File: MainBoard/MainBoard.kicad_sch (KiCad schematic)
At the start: 30 parts, among them J1 1761681-3, Q1 BC557, Q2 BC557, Q3 BC557, Q4 BC557, Q5 BC547, Q6 BC547, Q7 BC547, Q8 BC547

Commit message: snapshot
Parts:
- added R5: 470k, symbol Device:R
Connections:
- net NonInvertingInput: now also R5.1
- net Output: now also R5.2
- net DiffPair renamed InputStage
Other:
- moved on the sheet: D3, D4, D5, D6, Q1, Q2, Q3, Q4, Q5, Q6, Q7, Q8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

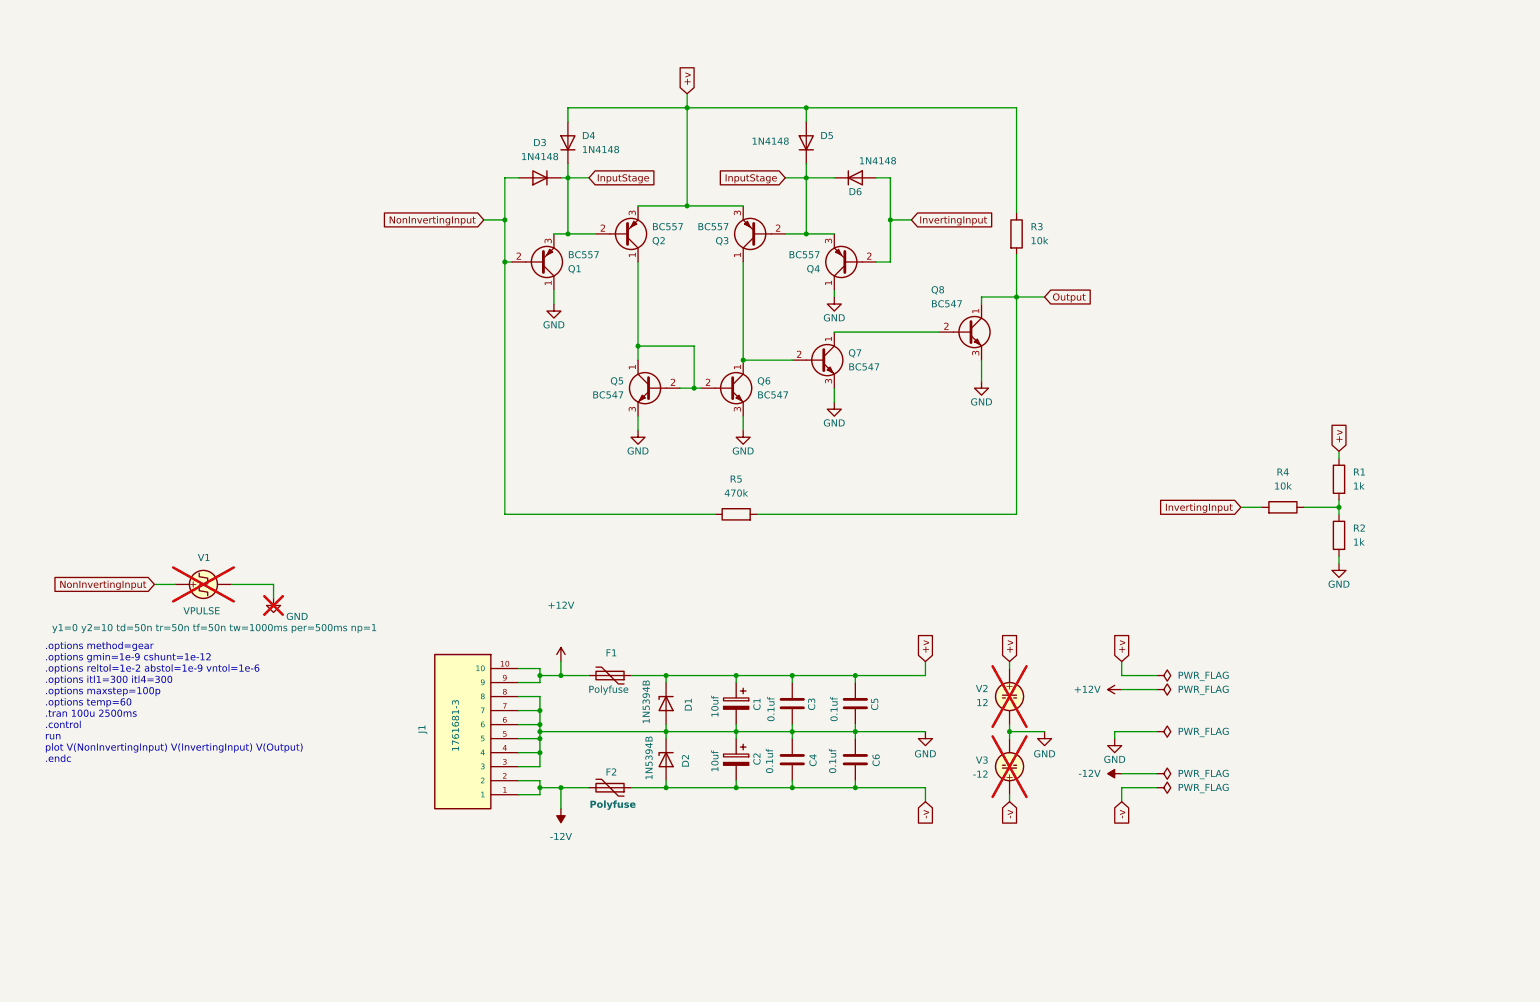
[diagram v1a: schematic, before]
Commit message: corrected input stage
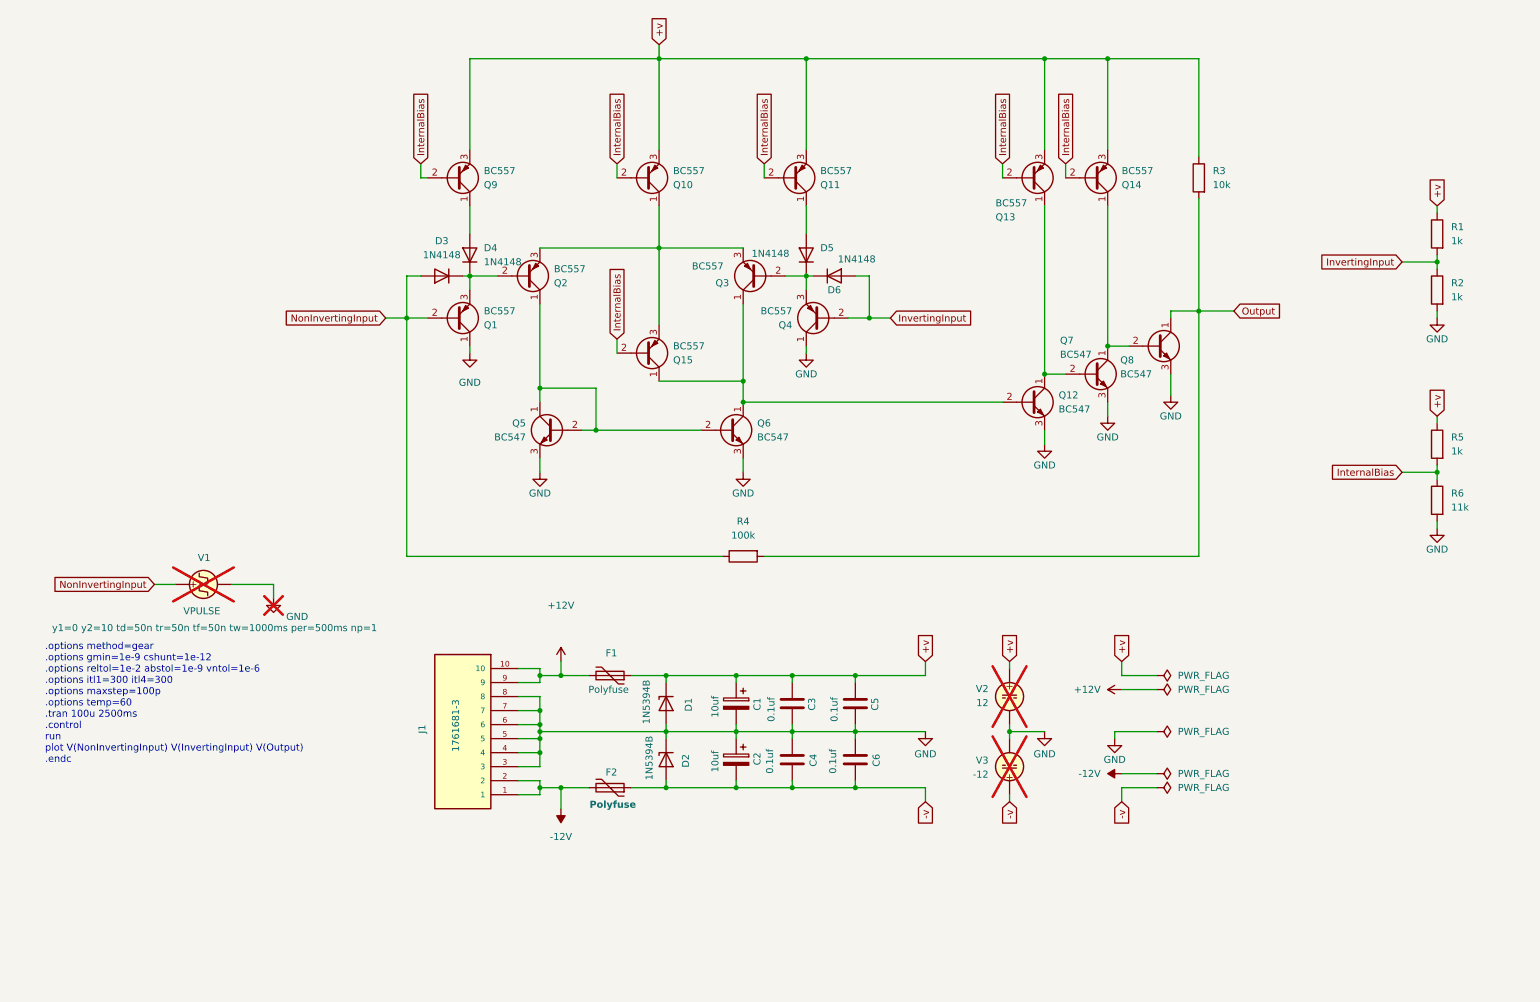
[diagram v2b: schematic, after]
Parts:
- added Q10, Q11, Q13, Q14, Q15, Q9: BC557, Package_TO_SOT_THT:TO-92_Inline, symbol Transistor_BJT:BC557
- added Q12: BC547, Package_TO_SOT_THT:TO-92_Inline, symbol Transistor_BJT:BC547
- added R6: 11k, symbol Device:R
- R4: value 10k -> 100k
- R5: value 470k -> 1k
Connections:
- net +v: now also R5.1, Q10.3 (E), Q11.3 (E), Q13.3 (E), Q14.3 (E), Q9.3 (E); no longer D4.2 (A), D5.2 (A), Q2.3 (E), Q3.3 (E)
- net GND: now also Q12.3 (E), R6.2
- net InvertingInput: now also R1.2, R2.1; no longer R4.2
- net NonInvertingInput: now also R4.1; no longer R5.1
- net Output: now also R4.2; no longer R5.2
- net at Q7.1 (C), Q8.2 (B): now also Q14.1 (C)
- net at Q3.1 (C), Q6.1 (C): now also Q12.2 (B), Q15.1 (C); no longer Q7.2 (B)
- net InputStage: no longer names the net of D3.1 (K), D4.1 (K), Q1.3 (E), Q2.2 (B)
- net InputStage: no longer D5.1 (K), D6.1 (K), Q3.2 (B), Q4.3 (E)
- new net: Q12.1 (C), Q13.1 (C), Q7.2 (B)
- new net: D4.2 (A), Q9.1 (C)
- new net: D5.1 (K), D6.1 (K), Q3.2 (B), Q4.3 (E)
- new net: Q10.1 (C), Q15.3 (E), Q2.3 (E), Q3.3 (E)
- new net: D5.2 (A), Q11.1 (C)
- new net InternalBias: Q10.2 (B), Q11.2 (B), Q13.2 (B), Q14.2 (B), Q15.2 (B), Q9.2 (B), R5.2, R6.1
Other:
- moved on the sheet: D3, D4, D5, D6, Q1, Q2, Q3, Q4, Q5, Q6, Q7, Q8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

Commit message: adjusted simulation paramters
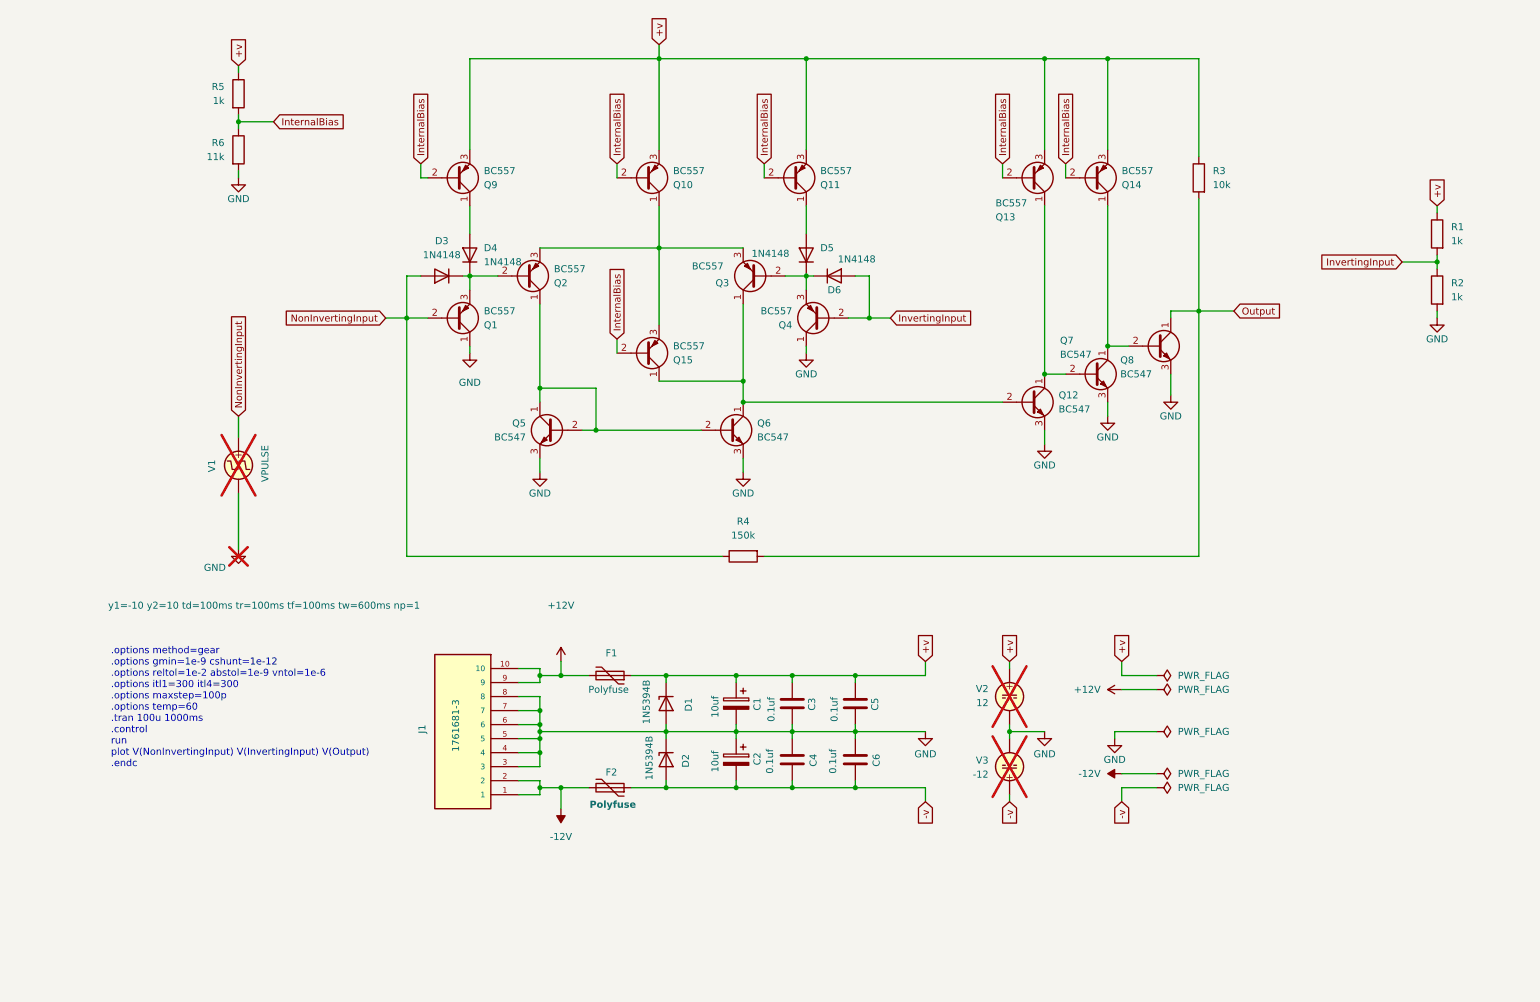
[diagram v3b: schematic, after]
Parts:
- R4: value 100k -> 150k
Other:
- note added: ".options method=gear .options gmin=1e-9 cshunt=1e-12 .options reltol=1e-2 abstol=1e-9 vntol=1e-6 .options itl1=300 itl4=300 .options maxstep=100p .options temp=60 .tran 100u 1000ms .control run plot V(NonInvertingInput) V(InvertingInput) V(Output) .endc"
- note removed: ".options method=gear .options gmin=1e-9 cshunt=1e-12 .options reltol=1e-2 abstol=1e-9 vntol=1e-6 .options itl1=300 itl4=300 .options maxstep=100p .options temp=60 .tran 100u 2500ms .control run plot V(NonInvertingInput) V(InvertingInput) V(Output) .endc"
- moved on the sheet: R5, R6, V1
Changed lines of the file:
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@@
 	(generator_version "9.0")
 	(paper "A4")
-	(text ".options method=gear \n.options gmin=1e-9 cshunt=1e-12 \n.options reltol=1e-2 abstol=1e-9 vntol=1e-6 \n.options itl1=300 itl4=300 \n.options maxstep=100p\n.options temp=60\n.tran 100u 2500ms\n.control\nrun\nplot V(NonInvertingInput) V(InvertingInput) V(Output)\n.endc"
+	(text ".options method=gear \n.options gmin=1e-9 cshunt=1e-12 \n.options reltol=1e-2 abstol=1e-9 vntol=1e-6 \n.options itl1=300 itl4=300 \n.options maxstep=100p\n.options temp=60\n.tran 100u 1000ms\n.control\nrun\nplot V(NonInvertingInput) V(InvertingInput) V(Output)\n.endc"
 		(exclude_from_sim no)
-		(at 19.558 138.43 0)
+		(at 31.496 139.192 0)
 		(effects
 			(font
@@
 	)
 	(junction
-		(at 271.78 96.52)
+		(at 54.61 33.02)
 		(diameter 0)
 		(color 0 0 0 0)
@@
 	(wire
 		(pts
-			(xy 271.78 96.52) (xy 265.43 96.52)
+			(xy 54.61 33.02) (xy 60.96 33.02)
 		)
 		(stroke
@@
 	(wire
 		(pts
-			(xy 60.96 116.84) (xy 60.96 119.38)
-		)
-		(stroke
-			(width 0)
-			(type default)
-		)
-	)
-	(wire
-		(pts
 			(xy 153.67 60.96) (xy 157.48 60.96)
 		)
@@
 	(wire
 		(pts
-			(xy 271.78 95.25) (xy 271.78 96.52)
+			(xy 54.61 31.75) (xy 54.61 33.02)
 		)
 		(stroke
@@
 	(wire
 		(pts
-			(xy 271.78 86.36) (xy 271.78 87.63)
+			(xy 54.61 22.86) (xy 54.61 24.13)
 		)
 		(stroke
@@
 	(wire
 		(pts
-			(xy 39.37 116.84) (xy 43.18 116.84)
+			(xy 54.61 86.36) (xy 54.61 90.17)
 		)
 		(stroke
@@
 	(wire
 		(pts
-			(xy 53.34 116.84) (xy 60.96 116.84)
+			(xy 54.61 100.33) (xy 54.61 110.49)
 		)
 		(stroke
@@
 	(wire
 		(pts
-			(xy 271.78 105.41) (xy 271.78 106.68)
+			(xy 54.61 41.91) (xy 54.61 43.18)
 		)
 		(stroke
@@
 	(wire
 		(pts
-			(xy 271.78 96.52) (xy 271.78 97.79)
+			(xy 54.61 33.02) (xy 54.61 34.29)
 		)
 		(stroke
@@
 	(global_label "+v"
 		(shape input)
-		(at 271.78 86.36 90)
+		(at 54.61 22.86 90)
 		(fields_autoplaced yes)
 		(effects
@@
 		)
 		(property "Intersheetrefs" "${INTERSHEET_REFS}"
-			(at 271.78 80.8348 90)
+			(at 54.61 17.3348 90)
 			(effects
 				(font
@@
 	(global_label "InternalBias"
 		(shape input)
-		(at 265.43 96.52 180)
+		(at 60.96 33.02 0)
 		(fields_autoplaced yes)
 		(effects
@@
 				(size 1.27 1.27)
 			)
-			(justify right)
+			(justify left)
 		)
 		(property "Intersheetrefs" "${INTERSHEET_REFS}"
-			(at 251.0754 96.52 0)
+			(at 75.3146 33.02 0)
 			(effects
 				(font
 					(size 1.27 1.27)
 				)
-				(justify right)
+				(justify left)
 				(hide yes)
 			)
@@
 	(global_label "NonInvertingInput"
 		(shape input)
-		(at 39.37 116.84 180)
+		(at 54.61 86.36 90)
 		(fields_autoplaced yes)
 		(effects
@@
 				(size 1.27 1.27)
 			)
-			(justify right)
+			(justify left)
 		)
 		(property "Intersheetrefs" "${INTERSHEET_REFS}"
-			(at 19.7541 116.84 0)
+			(at 54.61 66.7441 90)
 			(effects
 				(font
 					(size 1.27 1.27)
 				)
-				(justify right)
+				(justify left)
 				(hide yes)
 			)
@@
 	(symbol
 		(lib_id "Simulation_SPICE:VPULSE")
-		(at 48.26 116.84 90)
+		(at 54.61 95.25 0)
+		(mirror y)
 		(unit 1)
 		(exclude_from_sim no)
@@
 		(dnp yes)
 		(property "Reference" "V1"
-			(at 49.53 112.014 90)
+			(at 49.784 96.52 90)
 			(effects
 				(font
@@
 		)
 		(property "Value" "VPULSE"
-			(at 51.308 121.666 90)
+			(at 59.436 98.298 90)
 			(effects
 				(font
@@
 		)
 		(property "Footprint" ""
-			(at 48.26 116.84 0)
+			(at 54.61 95.25 0)
 			(effects
 				(font
@@
 		)
 		(property "Datasheet" "https://ngspice.sourceforge.io/docs/ngspice-html-manual/manual.xhtml#sec_Independent_Sources_for"
-			(at 48.26 116.84 0)
+			(at 54.61 95.25 0)
 			(effects
 				(font
@@
 		)
 		(property "Description" "Voltage source, pulse"
-			(at 48.26 116.84 0)
+			(at 54.61 95.25 0)
 			(effects
 				(font
@@
 		)
 		(property "Sim.Pins" "1=+ 2=-"
-			(at 48.26 116.84 0)
+			(at 54.61 95.25 0)
 			(effects
 				(font
@@
 		)
 		(property "Sim.Type" "PULSE"
-			(at 48.26 116.84 0)
+			(at 54.61 95.25 0)
 			(effects
 				(font
@@
 		)
 		(property "Sim.Device" "V"
-			(at 48.26 116.84 0)
+			(at 54.61 95.25 0)
 			(effects
 				(font
@@
 			)
 		)
-		(property "Sim.Params" "y1=0 y2=10 td=50n tr=50n tf=50n tw=1000ms per=500ms np=1"
-			(at 20.828 124.714 90)
+		(property "Sim.Params" "y1=-10 y2=10 td=100ms tr=100ms tf=100ms tw=600ms np=1"
+			(at 30.988 120.65 0)
 			(effects
 				(font
@@
 	(symbol
 		(lib_id "Device:R")
-		(at 271.78 101.6 0)
-		(mirror y)
+		(at 54.61 38.1 0)
 		(unit 1)
 		(exclude_from_sim no)
@@
 		(fields_autoplaced yes)
 		(property "Reference" "R6"
-			(at 274.32 100.3299 0)
+			(at 52.07 36.8299 0)
 			(effects
 				(font
@@
 		)
 		(property "Value" "11k"
-			(at 274.32 102.8699 0)
+			(at 52.07 39.3699 0)
 			(effects
 				(font
@@
 		)
 		(property "Footprint" ""
-			(at 273.558 101.6 90)
+			(at 52.832 38.1 90)
 			(effects
 				(font
@@
 		)
 		(property "Datasheet" "~"
-			(at 271.78 101.6 0)
+			(at 54.61 38.1 0)
 			(effects
 				(font
@@
 		)
 		(property "Description" "Resistor"
-			(at 271.78 101.6 0)
+			(at 54.61 38.1 0)
 			(effects
 				(font
@@
 	(symbol
 		(lib_id "power:GND")
-		(at 271.78 106.68 0)
-		(mirror y)
+		(at 54.61 43.18 0)
 		(unit 1)
 		(exclude_from_sim no)
@@
 		(dnp no)
 		(property "Reference" "#PWR017"
-			(at 271.78 113.03 0)
+			(at 54.61 49.53 0)
 			(effects
 				(font
@@
 		)
 		(property "Value" "GND"
-			(at 271.78 110.49 0)
+			(at 54.61 46.99 0)
 			(effects
 				(font
@@
 		)
 		(property "Footprint" ""
-			(at 271.78 106.68 0)
+			(at 54.61 43.18 0)
 			(effects
 				(font
@@
 		)
 		(property "Datasheet" ""
-			(at 271.78 106.68 0)
+			(at 54.61 43.18 0)
 			(effects
 				(font
@@
 		)
 		(property "Description" "Power symbol creates a global label with name \"GND\" , ground"
-			(at 271.78 106.68 0)
+			(at 54.61 43.18 0)
 			(effects
 				(font
@@
 	(symbol
 		(lib_id "power:GND")
-		(at 60.96 119.38 0)
+		(at 54.61 110.49 0)
+		(mirror y)
 		(unit 1)
 		(exclude_from_sim no)
@@
 		(dnp yes)
 		(property "Reference" "#PWR02"
-			(at 60.96 125.73 0)
+			(at 54.61 116.84 0)
 			(effects
 				(font
@@
 		)
 		(property "Value" "GND"
-			(at 63.246 122.682 0)
+			(at 52.324 113.792 0)
 			(effects
 				(font
@@
 		)
 		(property "Footprint" ""
-			(at 60.96 119.38 0)
+			(at 54.61 110.49 0)
 			(effects
 				(font
@@
 		)
 		(property "Datasheet" ""
-			(at 60.96 119.38 0)
+			(at 54.61 110.49 0)
 			(effects
 				(font
@@
 		)
 		(property "Description" "Power symbol creates a global label with name \"GND\" , ground"
-			(at 60.96 119.38 0)
+			(at 54.61 110.49 0)
 			(effects
 				(font
@@
 	(symbol
 		(lib_id "Device:R")
-		(at 271.78 91.44 0)
-		(mirror y)
+		(at 54.61 27.94 0)
 		(unit 1)
 		(exclude_from_sim no)
@@
 		(fields_autoplaced yes)
 		(property "Reference" "R5"
-			(at 274.32 90.1699 0)
+			(at 52.07 26.6699 0)
 			(effects
 				(font
@@
 		)
 		(property "Value" "1k"
-			(at 274.32 92.7099 0)
+			(at 52.07 29.2099 0)
 			(effects
 				(font
@@
 		)
 		(property "Footprint" ""
-			(at 273.558 91.44 90)
+			(at 52.832 27.94 90)
 			(effects
 				(font
@@
 		)
 		(property "Datasheet" "~"
-			(at 271.78 91.44 0)
+			(at 54.61 27.94 0)
 			(effects
 				(font
@@
 		)
 		(property "Description" "Resistor"
-			(at 271.78 91.44 0)
+			(at 54.61 27.94 0)
 			(effects
 				(font
@@
 			)
 		)
-		(property "Value" "100k"
+		(property "Value" "150k"
 			(at 146.05 107.95 90)
 			(effects

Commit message: added title
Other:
- title: (none) -> Discrete Comparator
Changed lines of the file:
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@@
 	(generator_version "9.0")
 	(paper "A4")
+	(title_block
+		(title "Discrete Comparator")
+		(date "2026-02-25")
+		(rev "0.1")
+	)
 	(text ".options method=gear \n.options gmin=1e-9 cshunt=1e-12 \n.options reltol=1e-2 abstol=1e-9 vntol=1e-6 \n.options itl1=300 itl4=300 \n.options maxstep=100p\n.options temp=60\n.tran 100u 1000ms\n.control\nrun\nplot V(NonInvertingInput) V(InvertingInput) V(Output)\n.endc"
 		(exclude_from_sim no)
